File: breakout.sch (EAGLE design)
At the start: 22 parts, among them IC2 REG1117, U4 FT232R

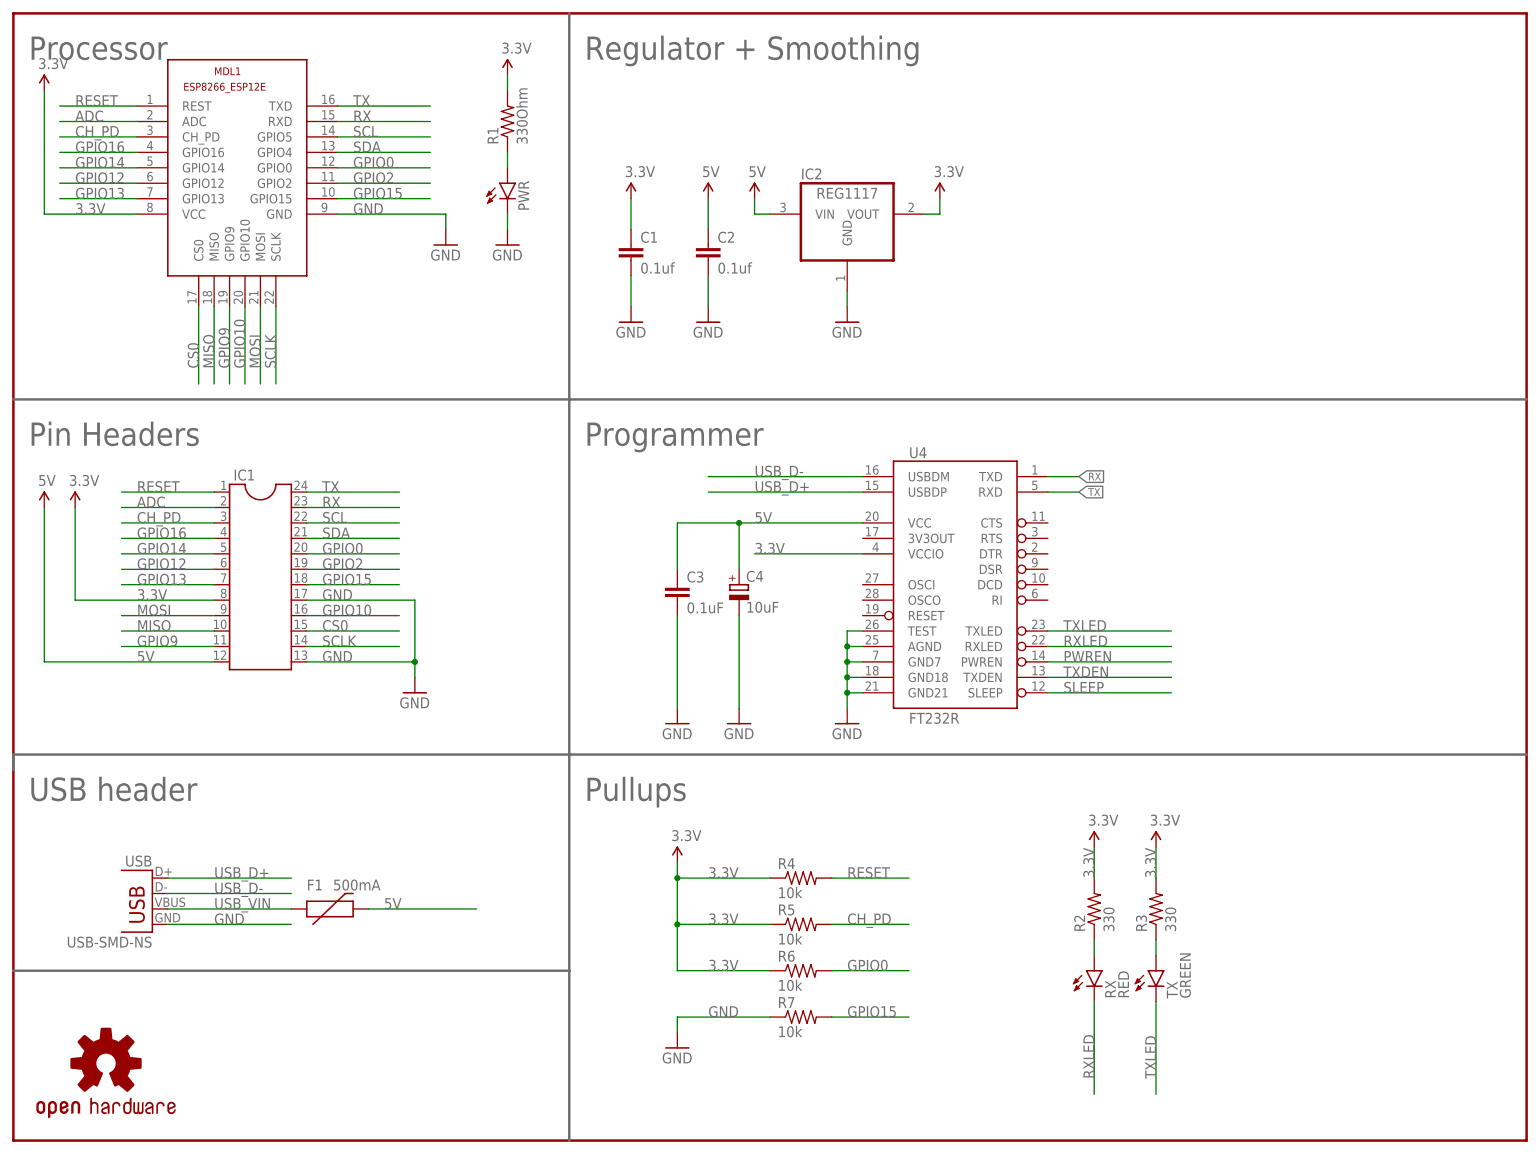
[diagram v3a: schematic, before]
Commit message: CH340G
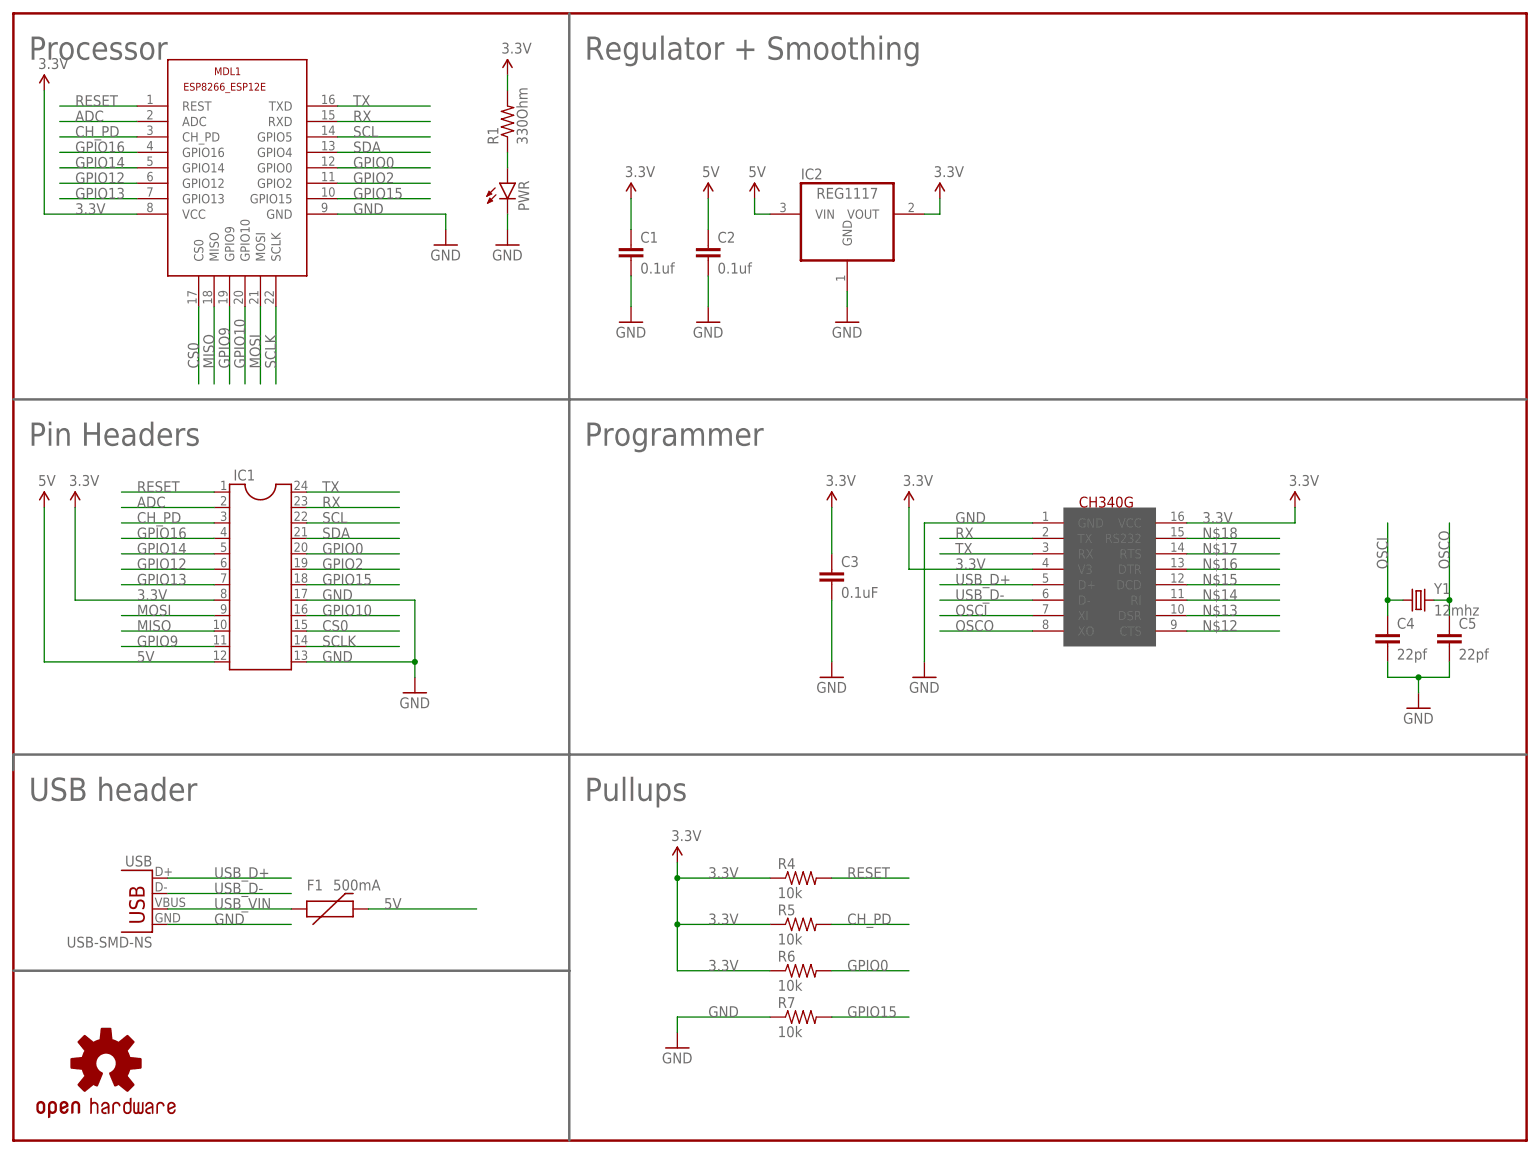
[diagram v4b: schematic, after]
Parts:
- removed R2, R3: 330, SparkFun-Passives:RESISTOR1206
- removed RX: RED, SparkFun-LED:LED1206
- removed TX: GREEN, SparkFun-LED:LED1206
- removed U4: FT232R, SparkFun:FT232RLSSOP
- added C5: 22pf, SparkFun-Capacitors:CAP1206
- added U$1: CH340G, CH340G-USB-SERIAL:CH340G
- added Y1: 12mhz, SparkFun-FreqCtrl:CRYSTALSMD
- C4: value 10uF -> 22pf; device rcl:CPOL-EUSMCA -> SparkFun-Capacitors:CAP1206
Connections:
- removed net N$2: R2.1, RX.A
- removed net N$3: R3.1, TX.A
- removed net PWREN: U4.PWREN
- removed net RXLED: RX.C, U4.RXLED
- removed net SLEEP: U4.SLEEP
- removed net TXDEN: U4.TXDEN
- removed net TXLED: TX.C, U4.TXLED
- new net N$12: U$1.CTS
- new net N$13: U$1.DSR
- new net N$14: U$1.RI
- new net N$15: U$1.DCD
- new net N$16: U$1.DTR
- new net N$17: U$1.RTS
- new net N$18: U$1.RS232
- new net OSCI: C4.1, U$1.XI, Y1.1
- new net OSCO: C5.1, U$1.XO, Y1.2
- net 3.3V: now also C3.1, U$1.V3, U$1.VCC; no longer R2.2, R3.2, U4.VCCIO
- net 5V: no longer C3.1, C4.+, U4.VCC
- net GND: now also C4.2, C5.2, U$1.GND; no longer C4.-, U4.AGND, U4.GND18, U4.GND21, U4.GND7, U4.TEST
- net RX: now also U$1.TX; no longer U4.TXD
- net TX: now also U$1.RX; no longer U4.RXD
- net USB_D+: now also U$1.D+; no longer U4.USBDP
- net USB_D-: now also U$1.D-; no longer U4.USBDM
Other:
- moved on the sheet: C3

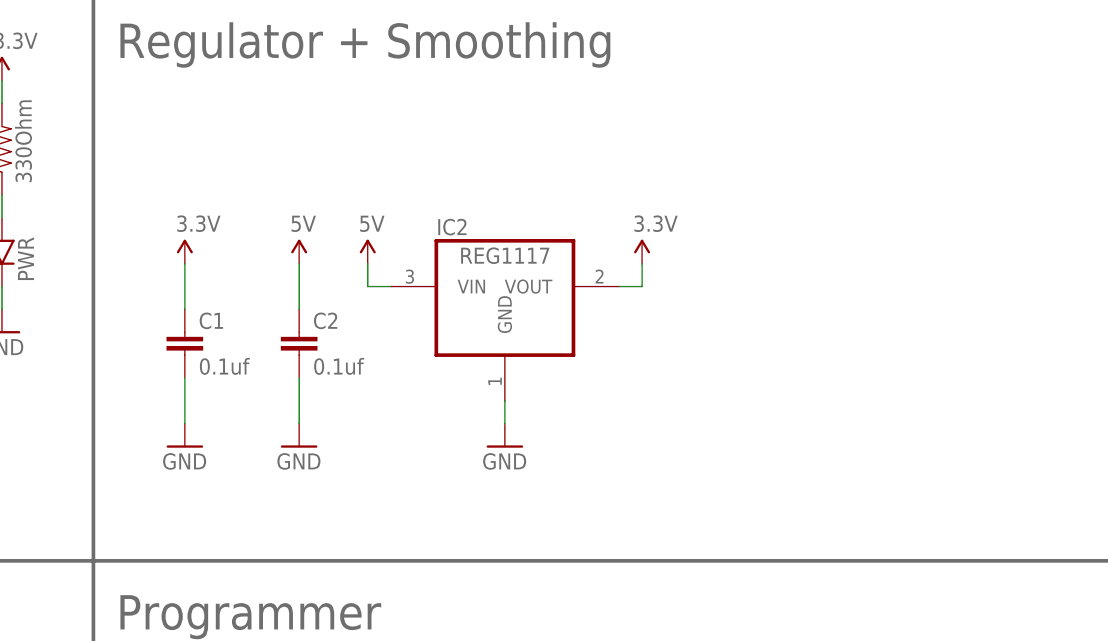
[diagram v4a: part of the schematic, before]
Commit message: Added a polarised 47uf size B capacitor to the 3.3v rail. Removed thermals from fill layers
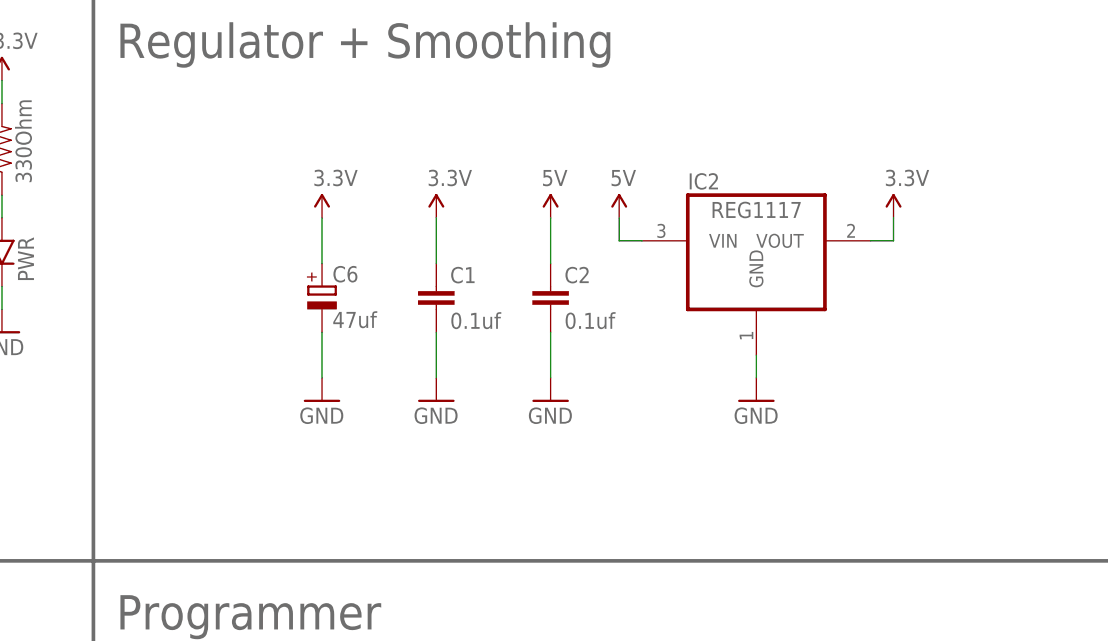
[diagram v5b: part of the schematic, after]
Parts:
- added C6: 47uf, rcl:CPOL-EUSMCB
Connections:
- net 3.3V: now also C6.+
- net GND: now also C6.-
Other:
- moved on the sheet: C1, C2, IC2
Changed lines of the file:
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@@
 <part name="C4" library="SparkFun-Capacitors" deviceset="CAP" device="1206" value="22pf"/>
 <part name="C5" library="SparkFun-Capacitors" deviceset="CAP" device="1206" value="22pf"/>
+<part name="GND11" library="supply1" deviceset="GND" device=""/>
+<part name="SUPPLY2" library="SparkFun-Aesthetics" deviceset="3.3V" device=""/>
+<part name="C6" library="rcl" deviceset="CPOL-EU" device="SMCB" value="47uf"/>
 </parts>
 <sheets>
@@
 <instance part="MDL1" gate="G$1" x="-2.54" y="121.92"/>
 <instance part="IC1" gate="G$1" x="-5.08" y="50.8"/>
-<instance part="C1" gate="G$1" x="55.88" y="104.14"/>
-<instance part="C2" gate="G$1" x="68.58" y="104.14"/>
+<instance part="C1" gate="G$1" x="83.82" y="109.22"/>
+<instance part="C2" gate="G$1" x="96.52" y="109.22"/>
 <instance part="GND2" gate="1" x="35.56" y="106.68"/>
 <instance part="GND3" gate="1" x="20.32" y="33.02"/>
-<instance part="GND4" gate="1" x="55.88" y="93.98"/>
+<instance part="GND4" gate="1" x="83.82" y="99.06"/>
 <instance part="GND5" gate="1" x="25.4" y="106.68"/>
-<instance part="GND6" gate="1" x="68.58" y="93.98"/>
-<instance part="GND7" gate="1" x="91.44" y="93.98"/>
+<instance part="GND6" gate="1" x="96.52" y="99.06"/>
+<instance part="GND7" gate="1" x="119.38" y="99.06"/>
 <instance part="GND8" gate="1" x="63.5" y="-25.4"/>
-<instance part="IC2" gate="G$1" x="91.44" y="111.76"/>
+<instance part="IC2" gate="G$1" x="119.38" y="116.84"/>
 <instance part="SUPPLY1" gate="G$1" x="35.56" y="134.62"/>
-<instance part="SUPPLY3" gate="G$1" x="106.68" y="114.3"/>
+<instance part="SUPPLY3" gate="G$1" x="134.62" y="119.38"/>
 <instance part="SUPPLY4" gate="G$1" x="-35.56" y="63.5"/>
-<instance part="SUPPLY5" gate="G$1" x="55.88" y="114.3"/>
+<instance part="SUPPLY5" gate="G$1" x="83.82" y="119.38"/>
 <instance part="SUPPLY6" gate="G$1" x="-40.64" y="132.08"/>
 <instance part="SUPPLY8" gate="G$1" x="63.5" y="5.08"/>
 <instance part="SUPPLY12" gate="G$1" x="-40.64" y="63.5"/>
-<instance part="SUPPLY13" gate="G$1" x="68.58" y="114.3"/>
-<instance part="SUPPLY14" gate="G$1" x="76.2" y="114.3"/>
+<instance part="SUPPLY13" gate="G$1" x="96.52" y="119.38"/>
+<instance part="SUPPLY14" gate="G$1" x="104.14" y="119.38"/>
 <instance part="PWR" gate="G$1" x="35.56" y="116.84"/>
 <instance part="R1" gate="G$1" x="35.56" y="127" rot="R90"/>
@@
 <instance part="C4" gate="G$1" x="180.34" y="40.64"/>
 <instance part="C5" gate="G$1" x="190.5" y="40.64"/>
+<instance part="GND11" gate="1" x="71.12" y="99.06"/>
+<instance part="SUPPLY2" gate="G$1" x="71.12" y="119.38"/>
+<instance part="C6" gate="G$1" x="71.12" y="111.76"/>
 </instances>
 <busses>
@@
 <segment>
 <pinref part="SUPPLY14" gate="G$1" pin="5V"/>
-<wire x1="76.2" y1="114.3" x2="76.2" y2="111.76" width="0.1524" layer="91"/>
+<wire x1="104.14" y1="119.38" x2="104.14" y2="116.84" width="0.1524" layer="91"/>
 <pinref part="IC2" gate="G$1" pin="VIN"/>
-<wire x1="76.2" y1="111.76" x2="78.74" y2="111.76" width="0.1524" layer="91"/>
+<wire x1="104.14" y1="116.84" x2="106.68" y2="116.84" width="0.1524" layer="91"/>
 </segment>
 <segment>
 <pinref part="SUPPLY13" gate="G$1" pin="5V"/>
 <pinref part="C2" gate="G$1" pin="1"/>
-<wire x1="68.58" y1="109.22" x2="68.58" y2="114.3" width="0.1524" layer="91"/>
+<wire x1="96.52" y1="114.3" x2="96.52" y2="119.38" width="0.1524" layer="91"/>
 </segment>
 <segment>
@@
 <segment>
 <pinref part="SUPPLY3" gate="G$1" pin="3.3V"/>
-<wire x1="106.68" y1="114.3" x2="106.68" y2="111.76" width="0.1524" layer="91"/>
+<wire x1="134.62" y1="119.38" x2="134.62" y2="116.84" width="0.1524" layer="91"/>
 <pinref part="IC2" gate="G$1" pin="VOUT"/>
-<wire x1="106.68" y1="111.76" x2="104.14" y2="111.76" width="0.1524" layer="91"/>
+<wire x1="134.62" y1="116.84" x2="132.08" y2="116.84" width="0.1524" layer="91"/>
 </segment>
 <segment>
 <pinref part="SUPPLY5" gate="G$1" pin="3.3V"/>
 <pinref part="C1" gate="G$1" pin="1"/>
-<wire x1="55.88" y1="109.22" x2="55.88" y2="114.3" width="0.1524" layer="91"/>
+<wire x1="83.82" y1="114.3" x2="83.82" y2="119.38" width="0.1524" layer="91"/>
 </segment>
 <segment>
@@
 <pinref part="C3" gate="G$1" pin="1"/>
 </segment>
+<segment>
+<pinref part="SUPPLY2" gate="G$1" pin="3.3V"/>
+<wire x1="71.12" y1="114.3" x2="71.12" y2="119.38" width="0.1524" layer="91"/>
+<pinref part="C6" gate="G$1" pin="+"/>
+</segment>
 </net>
 <net name="GPIO13" class="0">
@@
 <pinref part="IC2" gate="G$1" pin="GND"/>
 <pinref part="GND7" gate="1" pin="GND"/>
-<wire x1="91.44" y1="99.06" x2="91.44" y2="96.52" width="0.1524" layer="91"/>
+<wire x1="119.38" y1="104.14" x2="119.38" y2="101.6" width="0.1524" layer="91"/>
 </segment>
 <segment>
 <pinref part="GND4" gate="1" pin="GND"/>
 <pinref part="C1" gate="G$1" pin="2"/>
-<wire x1="55.88" y1="101.6" x2="55.88" y2="96.52" width="0.1524" layer="91"/>
+<wire x1="83.82" y1="106.68" x2="83.82" y2="101.6" width="0.1524" layer="91"/>
 </segment>
 <segment>
 <pinref part="GND6" gate="1" pin="GND"/>
 <pinref part="C2" gate="G$1" pin="2"/>
-<wire x1="68.58" y1="101.6" x2="68.58" y2="96.52" width="0.1524" layer="91"/>
+<wire x1="96.52" y1="106.68" x2="96.52" y2="101.6" width="0.1524" layer="91"/>
 </segment>
 <segment>
@@
 <junction x="185.42" y="35.56"/>
 </segment>
-</net>
+<segment>
+<pinref part="GND11" gate="1" pin="GND"/>
+<wire x1="71.12" y1="106.68" x2="71.12" y2="101.6" width="0.1524" layer="91"/>
+<pinref part="C6" gate="G$1" pin="-"/>
+</segment>
+</net>
